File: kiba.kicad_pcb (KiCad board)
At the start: 2 copper layers, 56.5 x 65 mm, 73 parts, among them IC1 TCA9548ARGERQ1, IC2 SGP40-D-R4, IC3 SGP40-D-R4, IC4 SGP40-D-R4, IC6 SGP40-D-R4, J1 Raspberry_Pi_2_3, Q1 2N7002NXAKR, U1 LM1117MP-3.3, U3 BMP581, U4 BMP581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

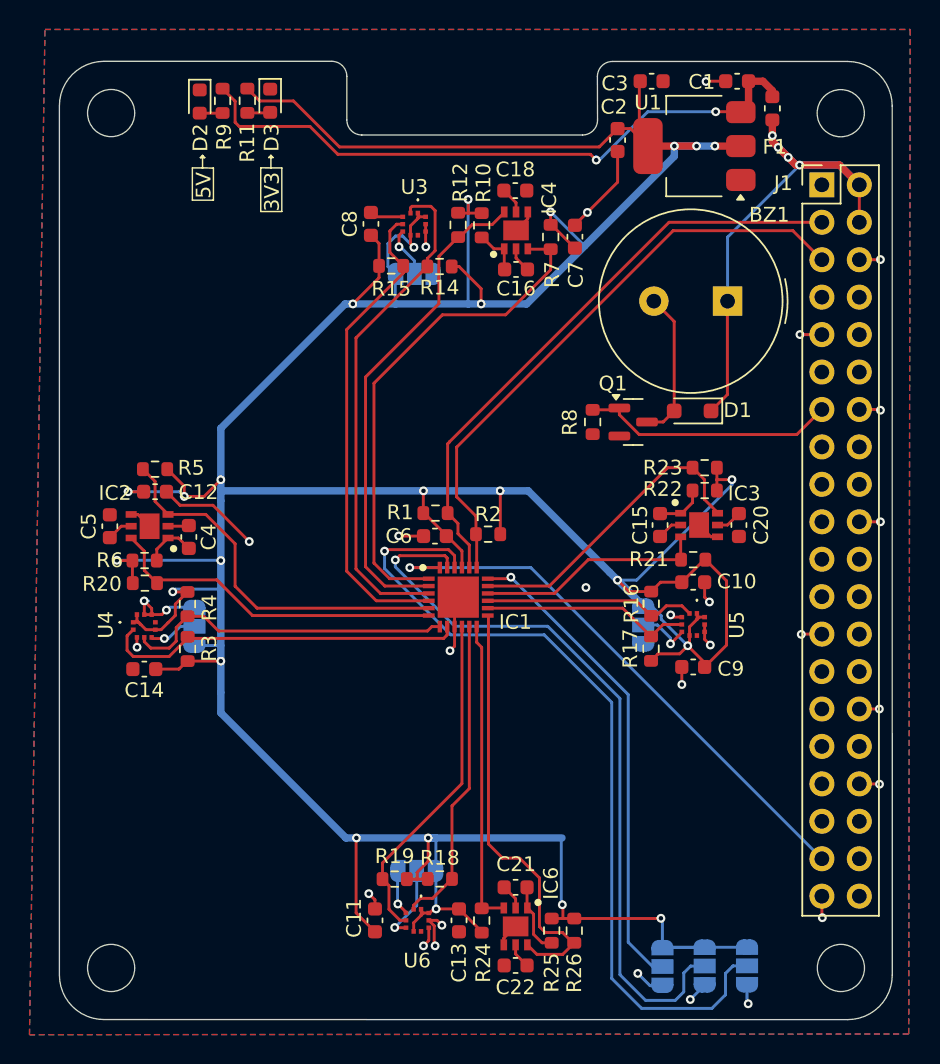
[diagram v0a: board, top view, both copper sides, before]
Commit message: fix: 4 channels i2c switch
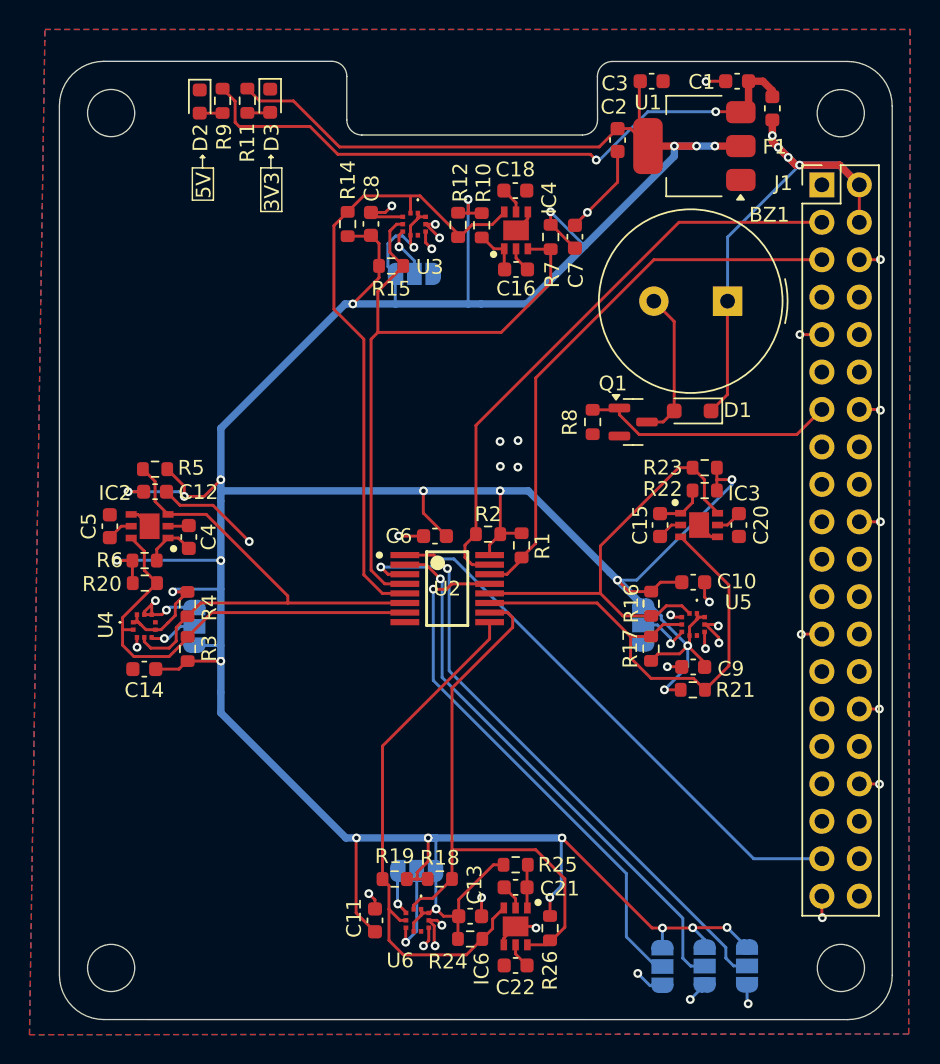
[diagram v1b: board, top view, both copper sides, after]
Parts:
- removed IC1: TCA9548ARGERQ1, Local:QFN50P400X400X100-25N-D
- added U2: TCA9546APWR, Local:PW0016A-IPC_A, F.Cu at (141.9, 105.5)
- moved R21 8.83 mm to (158.6, 112.3), turned to 0 degrees
- moved R14 6.87 mm to (135.1, 80.8), turned to 90 degrees
- moved R1 6.24 mm to (146.9, 102.5), turned to -90 degrees
- moved R25 5.09 mm to (146.5, 124.2), turned to 0 degrees
- moved R26 1.65 mm to (148.9, 128.5)
- moved R24 1.48 mm to (143.4, 129.2), turned to 0 degrees
- moved C13 0.81 mm to (143.4, 127.7), turned to 0 degrees
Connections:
- IC2 pad 3: /Sensors/SDA_GAS_2 -> /Sensors/SDA_1
- IC2 pad 6: /Sensors/SCL_GAS_2 -> /Sensors/SCK_1
- IC3 pad 3: /Sensors/SDA_GAS_3 -> /Sensors/SDA_2
- IC3 pad 6: /Sensors/SCL_GAS_3 -> /Sensors/SCK_2
- IC4 pad 3: /Sensors/SDA_GAS_1 -> /Sensors/SDA_0
- IC4 pad 6: /Sensors/SCL_GAS_1 -> /Sensors/SCK_0
- IC6 pad 3: /Sensors/SDA_GAS_4 -> /Sensors/SDA_3
- IC6 pad 6: /Sensors/SCL_GAS_4 -> /Sensors/SCK_3
- R1 pad 2: /Sensors/SDA -> /Sensors/SCK
- R12 pad 2: /Sensors/SCL_GAS_1 -> /Sensors/SCK_0
- R14 pad 2: /Sensors/SCK_PRESS_2 -> /Sensors/SCK_0
- R15 pad 2: /Sensors/SDA_PRESS_2 -> /Sensors/SDA_0
- R16 pad 2: /Sensors/SCK_PRESS_3 -> /Sensors/SCK_2
- R17 pad 2: /Sensors/SDA_PRESS_3 -> /Sensors/SDA_2
- R18 pad 2: /Sensors/SCK_PRESS_4 -> /Sensors/SCK_3
- R19 pad 2: /Sensors/SDA_PRESS_4 -> /Sensors/SDA_3
- R2 pad 2: /Sensors/SCK -> /Sensors/SDA
- R20 pad 2: /Sensors/SCL_GAS_2 -> /Sensors/SCK_1
- R21 pad 2: /Sensors/SDA_GAS_3 -> /Sensors/SDA_2
- R23 pad 2: /Sensors/SCL_GAS_3 -> /Sensors/SCK_2
- R24 pad 2: /Sensors/SDA_GAS_4 -> /Sensors/SDA_3
- R26 pad 2: /Sensors/SCL_GAS_4 -> /Sensors/SCK_3
- R3 pad 2: /Sensors/SCK_PRESS_1 -> /Sensors/SCK_1
- R4 pad 2: /Sensors/SDA_PRESS_1 -> /Sensors/SDA_1
- R5 pad 2: /Sensors/SDA_GAS_2 -> /Sensors/SDA_1
- R7 pad 2: /Sensors/SDA_GAS_1 -> /Sensors/SDA_0
- U3 pad 2: /Sensors/SCK_PRESS_2 -> /Sensors/SCK_0
- U3 pad 4: /Sensors/SDA_PRESS_2 -> /Sensors/SDA_0
- U4 pad 2: /Sensors/SCK_PRESS_1 -> /Sensors/SCK_1
- U4 pad 4: /Sensors/SDA_PRESS_1 -> /Sensors/SDA_1
- U5 pad 2: /Sensors/SCK_PRESS_3 -> /Sensors/SCK_2
- U5 pad 4: /Sensors/SDA_PRESS_3 -> /Sensors/SDA_2
- U6 pad 2: /Sensors/SCK_PRESS_4 -> /Sensors/SCK_3
- U6 pad 4: /Sensors/SDA_PRESS_4 -> /Sensors/SDA_3
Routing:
- net /Sensors/SDA_0: track 0.00 -> 45.0 mm
- net /Sensors/SCK_0: track 0.00 -> 43.4 mm
- net /Sensors/SCK_3: track 0.00 -> 39.7 mm
- net /Sensors/SDA_3: track 0.00 -> 36.1 mm
- net /Sensors/SDA_1: track 0.00 -> 34.6 mm
- net /Sensors/SDA_GAS_1: track 34.5 -> 0.00 mm
- net /Sensors/SCK_PRESS_2: track 34.4 -> 0.00 mm
- net /Sensors/SDA_2: track 0.00 -> 34.1 mm
- net /Sensors/SCL_GAS_1: track 33.7 -> 0.00 mm
- net /Sensors/SDA_PRESS_2: track 32.5 -> 0.00 mm
- net /Sensors/SCK_1: track 0.00 -> 30.5 mm
- net /Sensors/SCK_2: track 0.00 -> 30.2 mm
- net /Sensors/SCL_GAS_4: track 29.9 -> 0.00 mm
- net /Sensors/SDA_GAS_2: track 25.8 -> 0.00 mm
- net /Sensors/SCK_PRESS_1: track 24.9 -> 0.00 mm
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
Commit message: feat: add RH sensor
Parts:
- added C17: 100n, Capacitor_SMD:C_0603_1608Metric, F.Cu at (141.9, 100.4)
- added IC1: SHT40-CD1B-R3, Local:SHT40CD1BR3, F.Cu at (141.9, 103.2)
- added R13: 10k, Resistor_SMD:R_0603_1608Metric, F.Cu at (144.5, 102.7)
- added R27: 10k, Resistor_SMD:R_0603_1608Metric, F.Cu at (139.3, 103.7)
- moved R2 4.24 mm to (144.1, 106.0), turned to 0 degrees
- moved U2 4.22 mm to (141.9, 109.7)
- moved C6 4.07 mm to (141.1, 106.0)
- moved R1 0.96 mm to (146.0, 102.7)
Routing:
- net +3V3: track 329.7 -> 343.0 mm, vias 28 -> 30
- net /Sensors/SDA: track 40.4 -> 51.9 mm
- net /Sensors/SCK: track 38.0 -> 47.6 mm
- net /Sensors/SCK_3: track 39.7 -> 35.4 mm
- net /Sensors/SDA_0: track 45.0 -> 49.2 mm
- net /Sensors/SDA_3: track 36.1 -> 31.9 mm
- net /Sensors/SCK_0: track 43.4 -> 47.5 mm
- net /Sensors/A1: track 37.1 -> 33.4 mm
- net GND: track 71.3 -> 75.0 mm, vias 39 -> 95
- net /Sensors/A0: track 39.2 -> 35.6 mm
- net /Sensors/A2: track 36.3 -> 32.8 mm
- net /Sensors/SCK_2: track 30.2 -> 32.8 mm
- net /Sensors/SCK_1: track 30.5 -> 32.3 mm
- net /Sensors/SDA_1: track 34.6 -> 36.4 mm

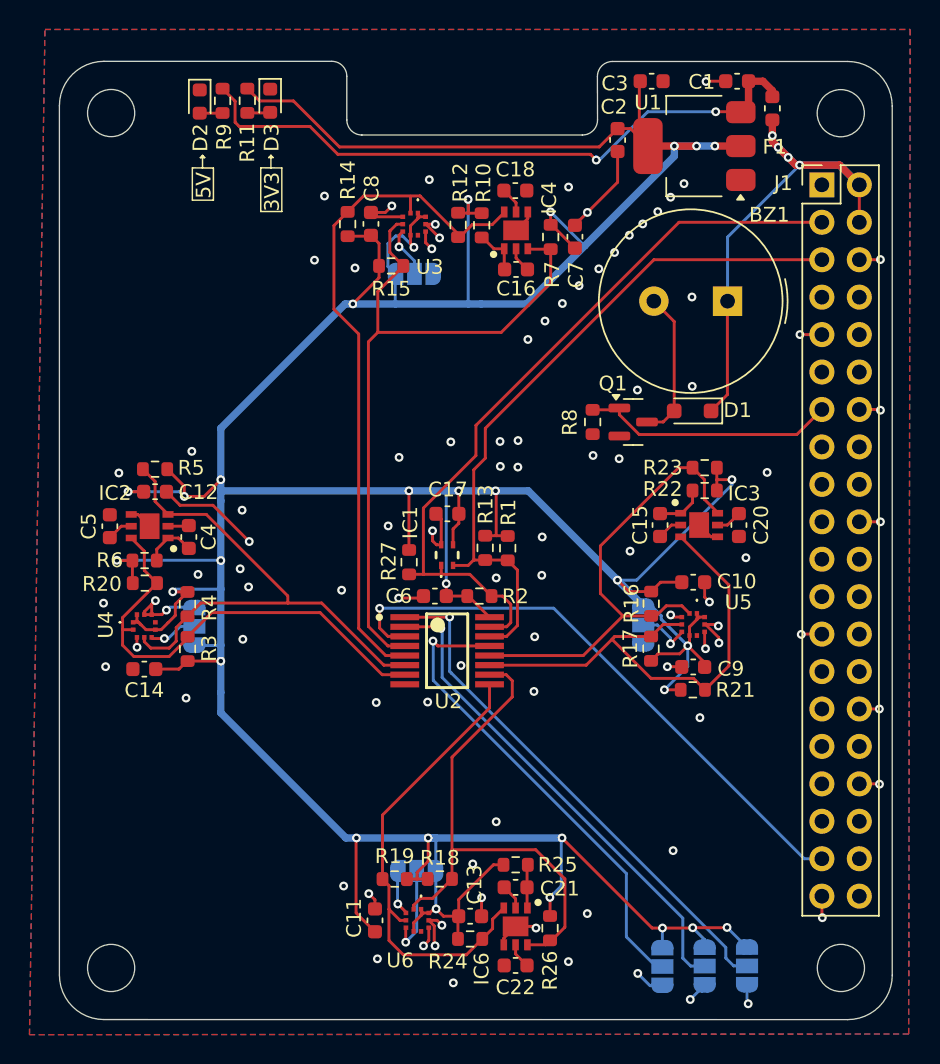
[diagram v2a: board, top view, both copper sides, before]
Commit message: fix: gnd zones clearane decreased
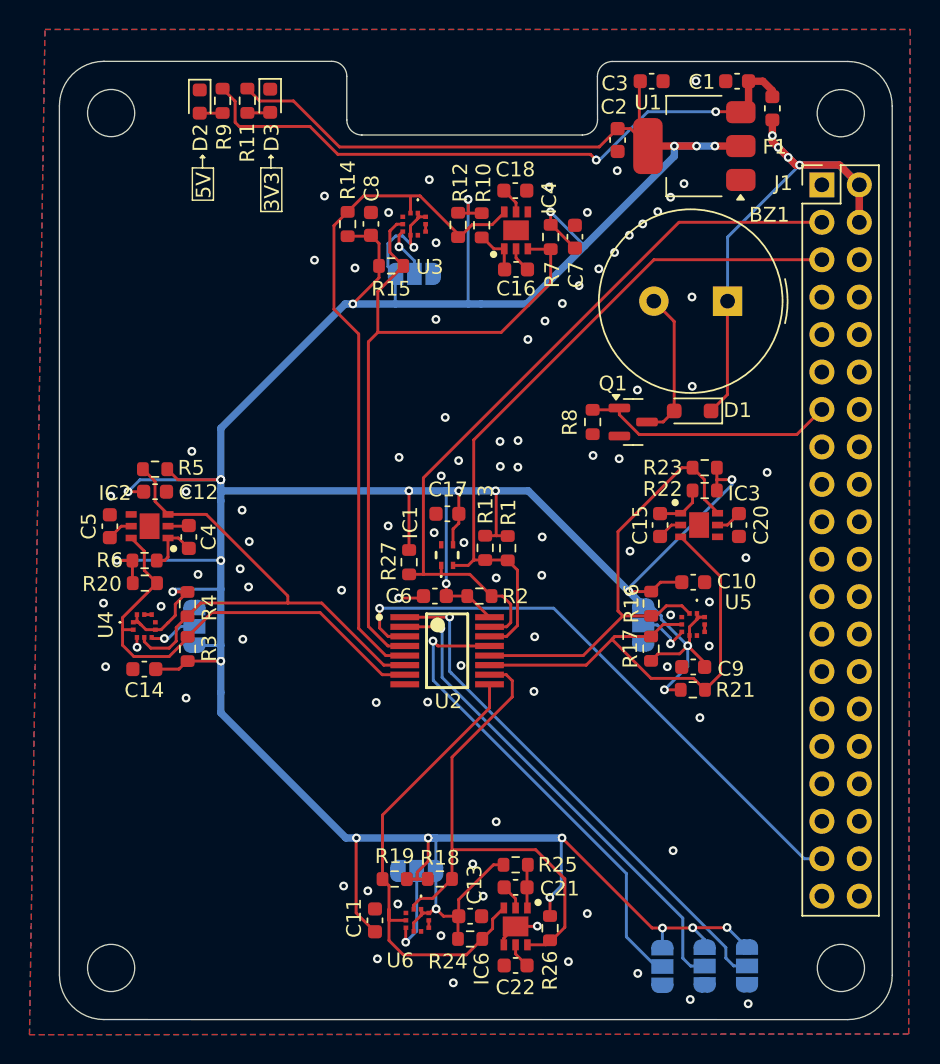
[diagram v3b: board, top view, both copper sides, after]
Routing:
- net GND: track 75.0 -> 7.93 mm, vias 95 -> 85
- net +5V: track 37.9 -> 40.4 mm
- net /Sensors/SCK_2: track 32.8 -> 31.7 mm
- net (no net): vias 0 -> 1

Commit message: fix: minors
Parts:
- moved R21 1.69 mm to (159.1, 110.8)
- moved C9 1.63 mm to (159.1, 112.3), turned to 0 degrees
- moved R24 1.59 mm to (143.4, 127.7)
- moved C13 1.48 mm to (143.4, 129.2)
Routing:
- net +3V3: track 342.9 -> 341.7 mm, vias 30 -> 29
- net /Sensors/SDA_2: track 34.1 -> 33.1 mm
- net GND: vias 85 -> 88
- net (no net): vias 1 -> 0

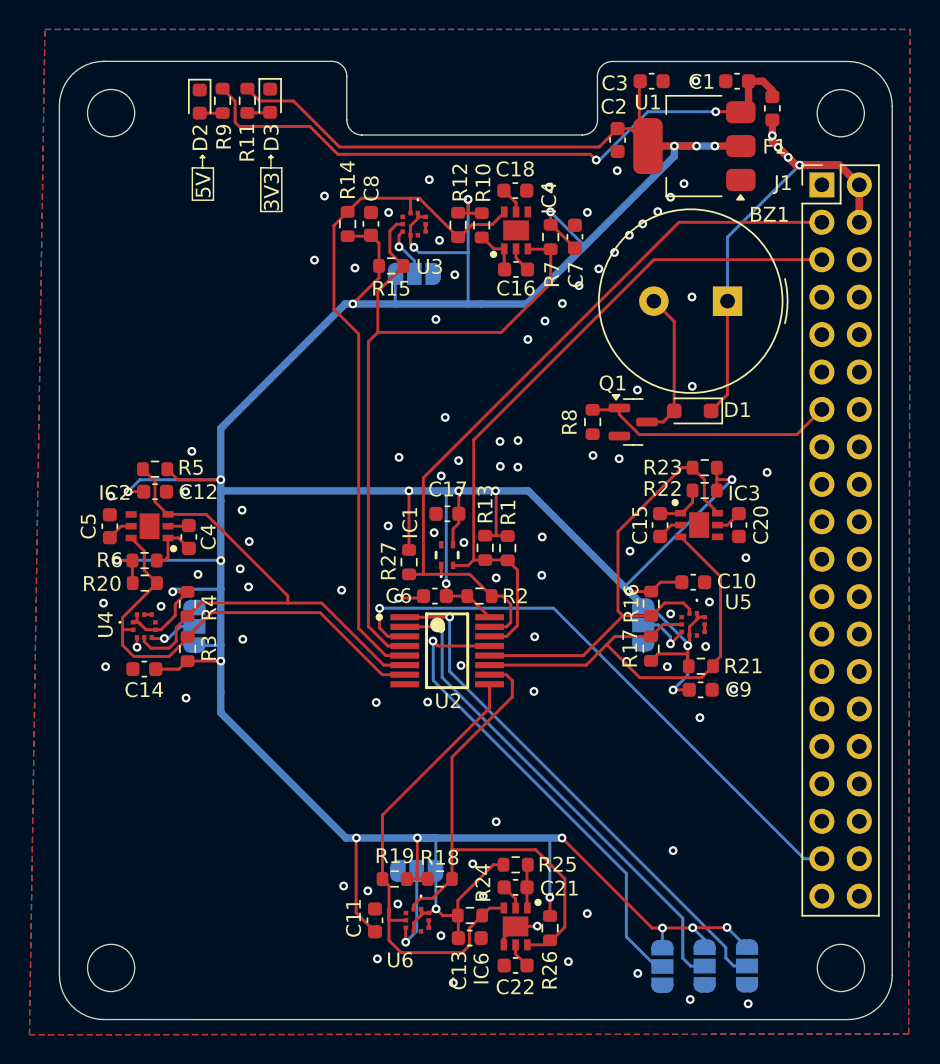
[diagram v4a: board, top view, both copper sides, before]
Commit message: fix: i2c layout with vias
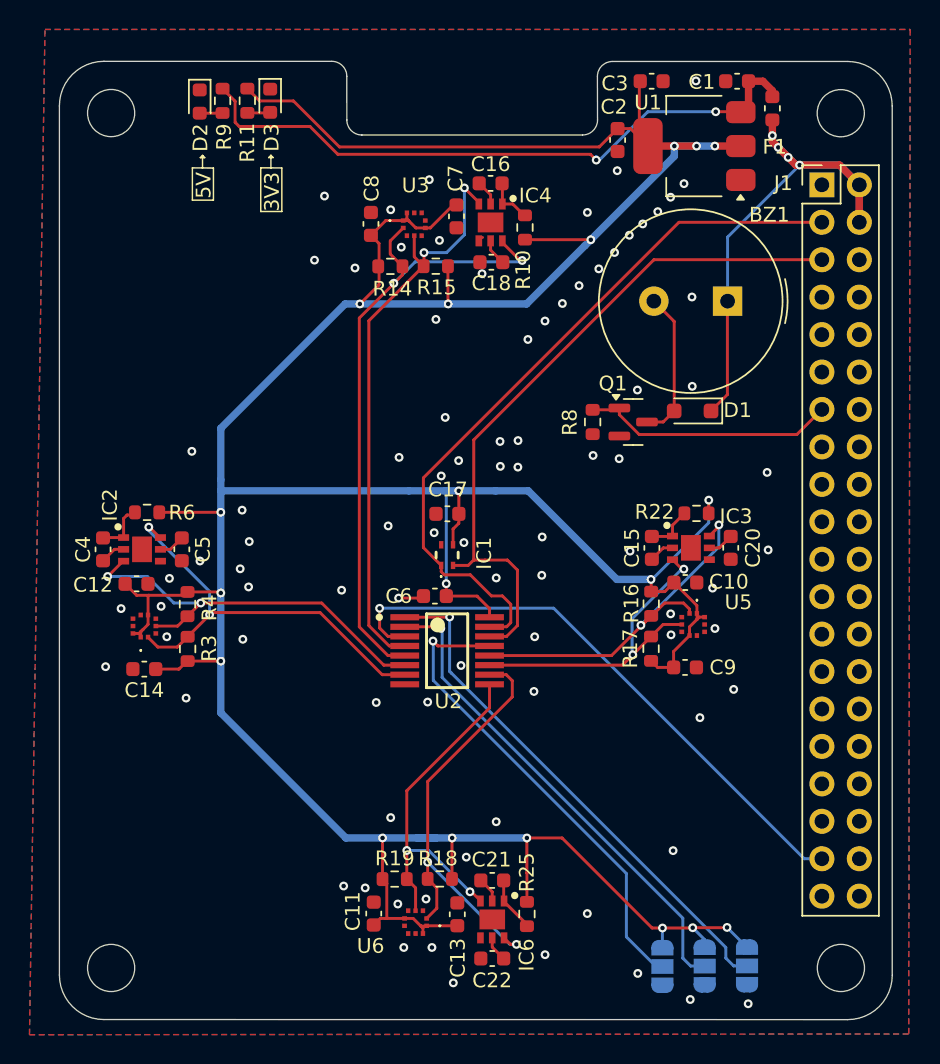
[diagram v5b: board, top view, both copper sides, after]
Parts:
- removed JP1, JP3, JP4, JP5: ADDRESS_SEL, Jumper:SolderJumper-3_P1.3mm_Open_RoundedPad1.0x1.5mm
- removed R1, R12, R2, R20, R21, R23, R24, R26, R5, R7: R, Resistor_SMD:R_0603_1608Metric
- removed R13, R27: 10k, Resistor_SMD:R_0603_1608Metric
- moved C7 8.15 mm to (142.5, 80.2), turned to -90 degrees
- moved C12 6.37 mm to (120.8, 105.2)
- moved C16 6.09 mm to (144.8, 78.0), turned to 180 degrees
- moved C4 5.88 mm to (118.5, 102.8), turned to -90 degrees
- moved C5 5.13 mm to (123.9, 102.8), turned to -90 degrees
- moved C18 5.12 mm to (144.9, 83.3), turned to 180 degrees
- moved R14 4.08 mm to (138.0, 83.6), turned to 0 degrees
- moved R25 3.43 mm to (147.3, 127.6), turned to -90 degrees
- moved R6 3.27 mm to (121.5, 100.3), turned to 180 degrees
- moved R15 3.03 mm to (141.1, 83.6), turned to 180 degrees
- moved R10 2.94 mm to (147.2, 81.0), turned to 90 degrees
- moved C9 1.85 mm to (158.0, 110.8)
- moved C13 1.82 mm to (142.6, 127.6), turned to 90 degrees
- moved IC4 1.81 mm to (144.8, 80.6), turned to -90 degrees
- moved C21 1.65 mm to (144.9, 125.3)
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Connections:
- U3 pad 5: Net-(JP3-C) -> GND
- U4 pad 5: Net-(JP1-C) -> GND
- U5 pad 5: Net-(JP4-C) -> GND
- U6 pad 5: Net-(JP5-C) -> GND
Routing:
- net +3V3: track 341.7 -> 276.0 mm, vias 29 -> 19
- net /Sensors/SDA_2: track 33.1 -> 22.6 mm, vias 0 -> 2
- net /Sensors/SDA_0: track 49.2 -> 40.1 mm, vias 0 -> 2
- net /Sensors/SDA_1: track 36.4 -> 27.9 mm, vias 0 -> 2
- net /Sensors/SDA_3: track 32.5 -> 24.4 mm, vias 0 -> 2
- net GND: track 7.93 -> 1.80 mm, vias 88 -> 87
- net Net-(JP5-C): track 6.13 -> 0.00 mm, vias 1 -> 0
- net /Sensors/SCK_2: track 32.0 -> 26.5 mm, vias 0 -> 2
- net /Sensors/SCK_3: track 35.4 -> 30.2 mm, vias 0 -> 2
- net Net-(JP4-C): track 3.79 -> 0.00 mm, vias 1 -> 0
- net Net-(JP3-C): track 3.47 -> 0.00 mm, vias 1 -> 0
- net Net-(JP1-C): track 3.27 -> 0.00 mm, vias 1 -> 0
- net /Sensors/SCK_1: track 32.3 -> 29.2 mm, vias 0 -> 2
- net /Sensors/SCK_0: track 47.1 -> 44.3 mm, vias 0 -> 2
- net /Sensors/SDA: track 51.9 -> 49.5 mm
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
